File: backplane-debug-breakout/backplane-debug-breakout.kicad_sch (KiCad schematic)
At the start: 14 parts, among them J1 Conn_02x08_Odd_Even, J2 Conn_01x04, J4 Conn_01x02_Socket, J5 Conn_01x04, J6 629105150521, SW1 SW_Push_DPDT, SW2 SW_Omron_B3FS, SW3 EG1218, U1 UMFT234XF

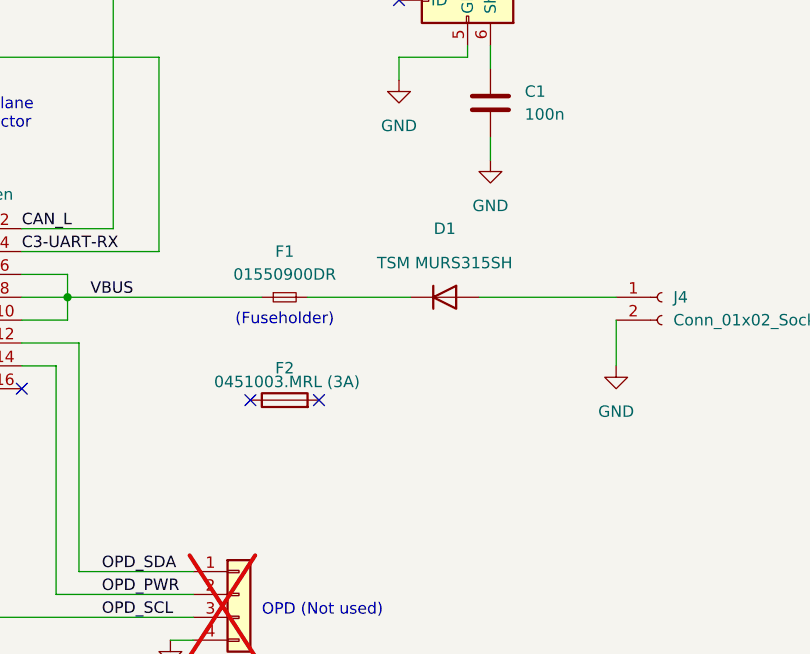
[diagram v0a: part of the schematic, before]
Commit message: added LED to schematic and modified pcb
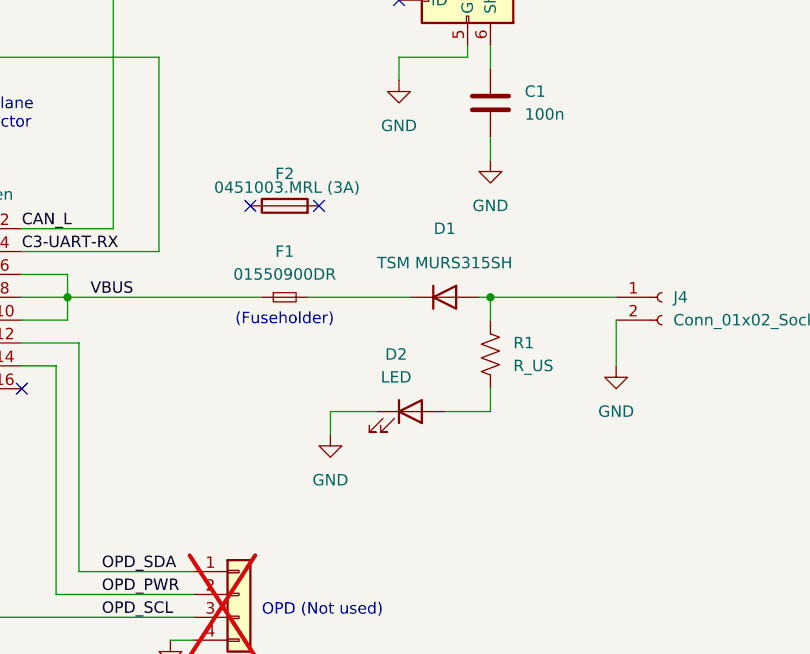
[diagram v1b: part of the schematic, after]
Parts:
- added D2: LED, LED_SMD:LED_0603_1608Metric_Pad1.05x0.95mm_HandSolder, symbol Device:LED
- added R1: R_US, Resistor_SMD:R_0603_1608Metric_Pad0.98x0.95mm_HandSolder, symbol Device:R_US
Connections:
- net GND: now also D2.1 (K)
- net at D1.2 (A), J4.1 (Pin_1): now also R1.1
- new net: D2.2 (A), R1.2
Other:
- moved on the sheet: F2

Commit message: finished
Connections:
- net VBUS: now also R1.1
- net at D1.2 (A), J4.1 (Pin_1): no longer R1.1
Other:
- moved on the sheet: D2, R1
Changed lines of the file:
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@@
+	)
+	(junction
+		(at 172.72 97.79)
+		(diameter 0)
+		(color 0 0 0 0)
 	)
 	(junction
@@
 	)
 	(junction
-		(at 204.47 97.79)
-		(diameter 0)
-		(color 0 0 0 0)
-	)
-	(junction
 		(at 157.48 97.79)
 		(diameter 0)
@@
 	(wire
 		(pts
+			(xy 172.72 97.79) (xy 179.07 97.79)
+		)
+		(stroke
+			(width 0)
+			(type default)
+		)
+	)
+	(wire
+		(pts
 			(xy 137.16 100.33) (xy 137.16 102.87)
 		)
@@
 	(wire
 		(pts
+			(xy 163.83 110.49) (xy 168.91 110.49)
+		)
+		(stroke
+			(width 0)
+			(type default)
+		)
+	)
+	(wire
+		(pts
 			(xy 158.75 102.87) (xy 158.75 128.27)
 		)
@@
 	(wire
 		(pts
-			(xy 157.48 97.79) (xy 179.07 97.79)
+			(xy 157.48 97.79) (xy 172.72 97.79)
 		)
 		(stroke
@@
 	(wire
 		(pts
+			(xy 172.72 106.68) (xy 176.53 106.68)
+		)
+		(stroke
+			(width 0)
+			(type default)
+		)
+	)
+	(wire
+		(pts
 			(xy 73.66 90.17) (xy 96.52 90.17)
 		)
@@
 	(wire
 		(pts
-			(xy 204.47 107.95) (xy 204.47 110.49)
-		)
-		(stroke
-			(width 0)
-			(type default)
-		)
-	)
-	(wire
-		(pts
 			(xy 218.44 100.33) (xy 218.44 105.41)
 		)
@@
 	(wire
 		(pts
-			(xy 191.77 110.49) (xy 186.69 110.49)
-		)
-		(stroke
-			(width 0)
-			(type default)
-		)
-	)
-	(wire
-		(pts
-			(xy 204.47 97.79) (xy 204.47 100.33)
+			(xy 172.72 97.79) (xy 172.72 99.06)
 		)
 		(stroke
@@
 	(wire
 		(pts
-			(xy 199.39 110.49) (xy 204.47 110.49)
-		)
-		(stroke
-			(width 0)
-			(type default)
-		)
-	)
-	(wire
-		(pts
 			(xy 102.87 46.99) (xy 143.51 46.99)
 		)
@@
 	(wire
 		(pts
-			(xy 204.47 97.79) (xy 218.44 97.79)
+			(xy 203.2 97.79) (xy 218.44 97.79)
+		)
+		(stroke
+			(width 0)
+			(type default)
+		)
+	)
+	(wire
+		(pts
+			(xy 176.53 106.68) (xy 176.53 110.49)
 		)
 		(stroke
@@
 	(wire
 		(pts
-			(xy 203.2 97.79) (xy 204.47 97.79)
-		)
-		(stroke
-			(width 0)
-			(type default)
-		)
-	)
-	(wire
-		(pts
-			(xy 186.69 110.49) (xy 186.69 113.03)
+			(xy 163.83 110.49) (xy 163.83 113.03)
 		)
 		(stroke
@@
 	(symbol
 		(lib_id "Device:LED")
-		(at 195.58 110.49 0)
+		(at 172.72 110.49 0)
 		(unit 1)
 		(exclude_from_sim no)
@@
 		(on_board yes)
 		(dnp no)
-		(fields_autoplaced yes)
 		(property "Reference" "D2"
-			(at 193.9925 104.14 0)
+			(at 172.72 113.792 0)
 			(effects
 				(font
@@
 		)
 		(property "Value" "LED"
-			(at 193.9925 106.68 0)
+			(at 172.72 116.332 0)
 			(effects
 				(font
@@
 		)
 		(property "Footprint" "LED_SMD:LED_0603_1608Metric_Pad1.05x0.95mm_HandSolder"
-			(at 195.58 110.49 0)
+			(at 172.72 110.49 0)
 			(effects
 				(font
@@
 		)
 		(property "Datasheet" "~"
-			(at 195.58 110.49 0)
+			(at 172.72 110.49 0)
 			(effects
 				(font
@@
 		)
 		(property "Description" "Light emitting diode"
-			(at 195.58 110.49 0)
+			(at 172.72 110.49 0)
 			(effects
 				(font
@@
 		(lib_name "GND_1")
 		(lib_id "power:GND")
-		(at 186.69 113.03 0)
+		(at 163.83 113.03 0)
 		(unit 1)
 		(exclude_from_sim no)
@@
 		(fields_autoplaced yes)
 		(property "Reference" "#PWR09"
-			(at 186.69 119.38 0)
+			(at 163.83 119.38 0)
 			(effects
 				(font
@@
 		)
 		(property "Value" "GND"
-			(at 186.69 118.11 0)
+			(at 163.83 118.11 0)
 			(effects
 				(font
@@
 		)
 		(property "Footprint" ""
-			(at 186.69 113.03 0)
+			(at 163.83 113.03 0)
 			(effects
 				(font
@@
 		)
 		(property "Datasheet" ""
-			(at 186.69 113.03 0)
+			(at 163.83 113.03 0)
 			(effects
 				(font
@@
 		)
 		(property "Description" "Power symbol creates a global label with name \"GND\" , ground"
-			(at 186.69 113.03 0)
+			(at 163.83 113.03 0)
 			(effects
 				(font
@@
 	(symbol
 		(lib_id "Device:R_US")
-		(at 204.47 104.14 0)
+		(at 172.72 102.87 0)
 		(unit 1)
 		(exclude_from_sim no)
@@
 		(fields_autoplaced yes)
 		(property "Reference" "R1"
-			(at 207.01 102.8699 0)
+			(at 175.26 101.5999 0)
 			(effects
 				(font
@@
 		)
 		(property "Value" "R_US"
-			(at 207.01 105.4099 0)
+			(at 175.26 104.1399 0)
 			(effects
 				(font
@@
 		)
 		(property "Footprint" "Resistor_SMD:R_0603_1608Metric_Pad0.98x0.95mm_HandSolder"
-			(at 205.486 104.394 90)
+			(at 173.736 103.124 90)
 			(effects
 				(font
@@
 		)
 		(property "Datasheet" "~"
-			(at 204.47 104.14 0)
+			(at 172.72 102.87 0)
 			(effects
 				(font
@@
 		)
 		(property "Description" "Resistor, US symbol"
-			(at 204.47 104.14 0)
-			(effects
-				(font
+			(at 172.72 102.87 0)
+			(effects
+				(font

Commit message: finished schematic, updated pcb
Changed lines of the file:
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@@
 	(text "momentary button and slide \nswitch for ~{SHUTDOWN}"
 		(exclude_from_sim no)
-		(at 80.01 87.376 0)
+		(at 80.01 87.63 0)
 		(effects
 			(font
@@
 	(text "add spacing to pins"
 		(exclude_from_sim no)
-		(at 110.236 42.672 0)
+		(at 110.49 43.18 0)
 		(effects
 			(font

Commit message: updated BOM
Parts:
- J4: DPN (none) -> 277-6718-ND; DST (none) -> Digi-Key; MFR (none) -> Phoenix; MPN (none) -> 1995499
- J6: DPN (none) -> 732-5960-1-ND; DST (none) -> Digi-Key
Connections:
- net GND: now also J4.1 (Pin_1); no longer J4.2 (Pin_2)
- net at D1.2 (A): now also J4.2 (Pin_2); no longer J4.1 (Pin_1)
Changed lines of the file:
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@@
+			)
+		)
+		(property "DPN" "732-5960-1-ND"
+			(at 201.93 59.69 0)
+			(effects
+				(font
+					(size 1.27 1.27)
+				)
+				(hide yes)
+			)
+		)
+		(property "DST" "Digi-Key"
+			(at 201.93 59.69 0)
+			(effects
+				(font
+					(size 1.27 1.27)
+				)
+				(hide yes)
 			)
 		)
@@
 	(symbol
 		(lib_id "Connector:Conn_01x02_Socket")
-		(at 223.52 97.79 0)
+		(at 223.52 100.33 0)
+		(mirror x)
 		(unit 1)
 		(exclude_from_sim no)
@@
 		(on_board yes)
 		(dnp no)
-		(fields_autoplaced yes)
 		(property "Reference" "J4"
-			(at 224.79 97.7899 0)
+			(at 224.79 100.3301 0)
 			(effects
 				(font
@@
 		)
 		(property "Value" "Conn_01x02_Socket"
-			(at 224.79 100.3299 0)
+			(at 224.79 97.7901 0)
 			(effects
 				(font
@@
 		)
 		(property "Footprint" "oresat-connectors:PHOENIX_1995499"
-			(at 223.52 97.79 0)
+			(at 223.52 100.33 0)
 			(effects
 				(font
@@
 		)
 		(property "Datasheet" "~"
-			(at 223.52 97.79 0)
+			(at 223.52 100.33 0)
 			(effects
 				(font
@@
 		)
 		(property "Description" "Generic connector, single row, 01x02, script generated"
-			(at 223.52 97.79 0)
+			(at 223.52 100.33 0)
 			(effects
 				(font
+					(size 1.27 1.27)
+				)
+				(hide yes)
+			)
+		)
+		(property "DPN" "277-6718-ND"
+			(at 223.52 100.33 0)
+			(effects
+				(font
+					(size 1.27 1.27)
+				)
+				(hide yes)
+			)
+		)
+		(property "DST" "Digi-Key"
+			(at 223.52 100.33 0)
+			(effects
+				(font
+					(size 1.27 1.27)
+				)
+				(hide yes)
+			)
+		)
+		(property "MFR" "Phoenix "
+			(at 223.52 100.33 0)
+			(effects
+				(font
+					(size 1.27 1.27)
+				)
+				(hide yes)
+			)
+		)
+		(property "MPN" "1995499"
+			(at 223.52 100.33 0)
+			(effects
+				(font

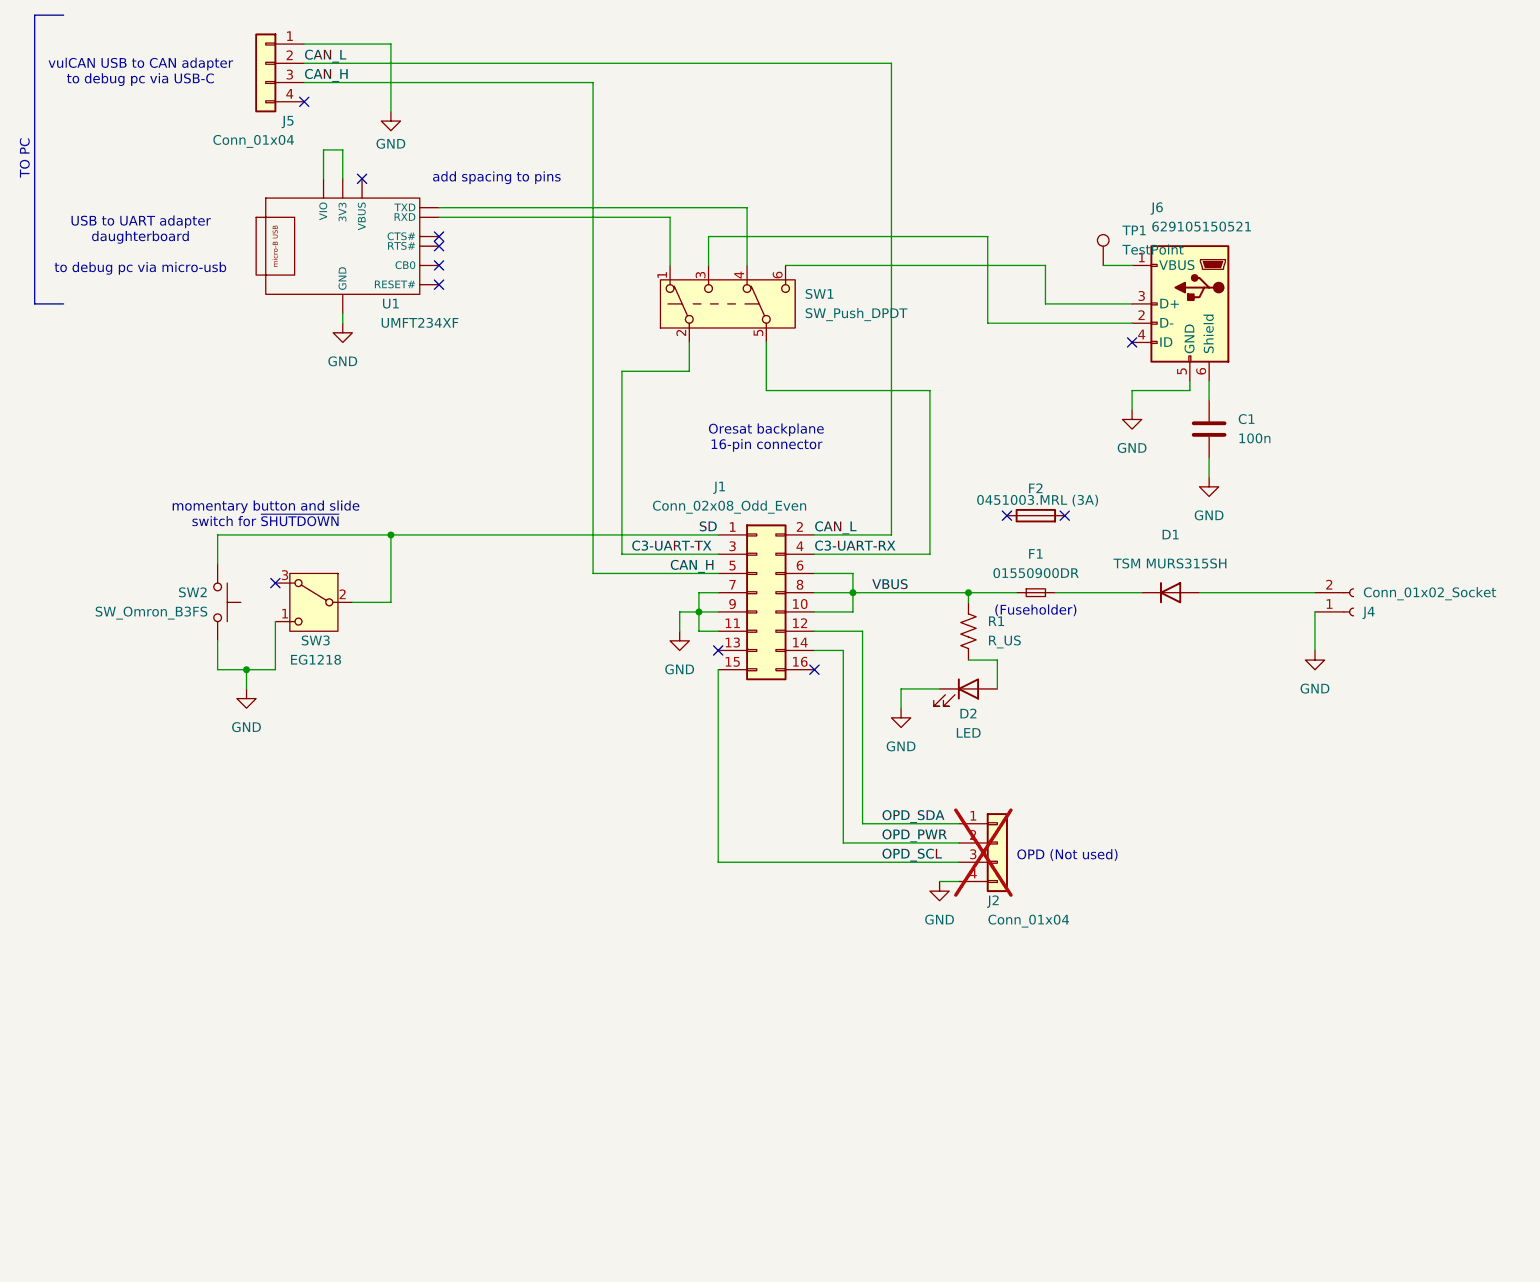
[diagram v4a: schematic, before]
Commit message: Board polish; updated design rules, made all inputs on the right, centered oresat connector, etc etc. Still needs an actual DPDT switch.
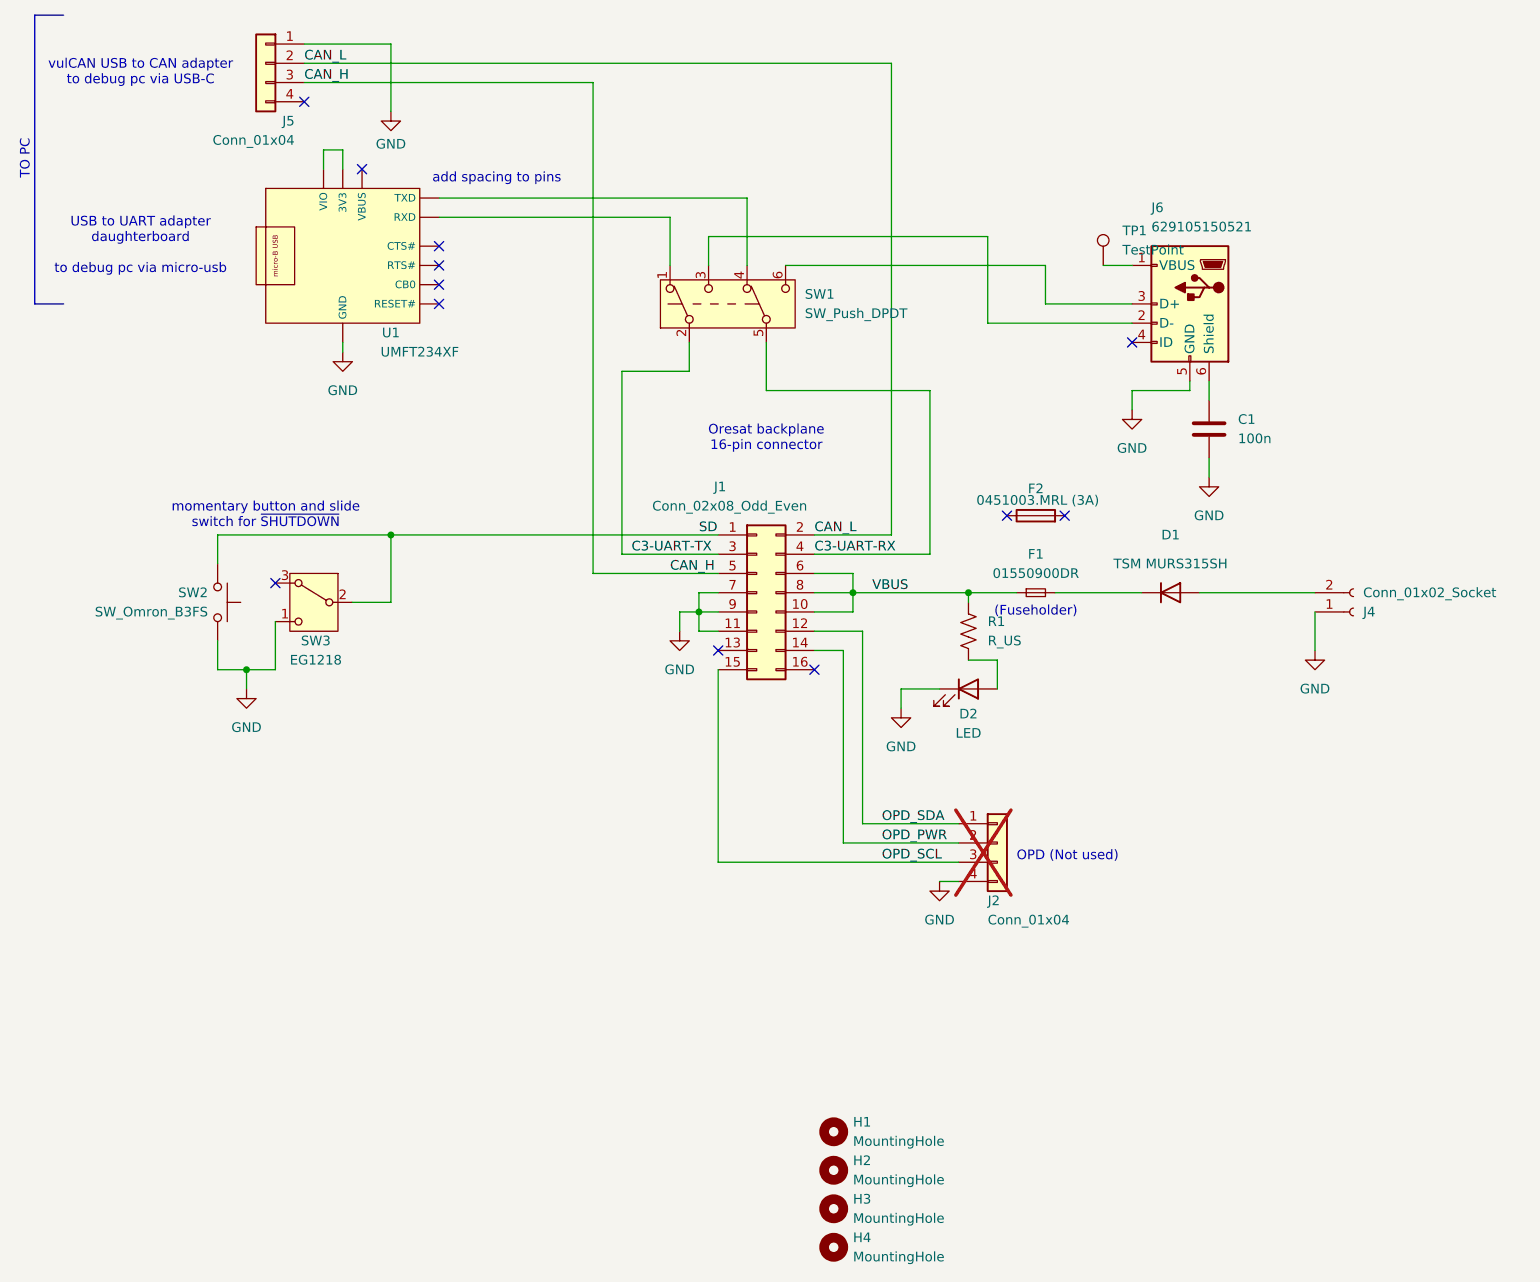
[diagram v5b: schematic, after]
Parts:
- added H1, H2, H3, H4: MountingHole, oresat-misc:MountingHole_3mm_no_copper, symbol Mechanical:MountingHole
- U1: footprint oresat-misc:UMFT234XF -> oresat-pcbs:UMFT234XF
